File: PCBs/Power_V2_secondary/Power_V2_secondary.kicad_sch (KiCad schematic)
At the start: 15 parts, among them IC7 ACS712ELCTR-20A-T, J1 PCIE-164-02-F-D-TH-TR, J2 Conn_01x08, J8 Conn_01x02, U1 01530007Z

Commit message: follow up changes from meeting
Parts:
- removed J2: Conn_01x08, TerminalBlock:TerminalBlock_MaiXu_MX126-5.0-08P_1x08_P5.00mm, symbol Connector_Generic:Conn_01x08
- added J2: Conn_01x10, TerminalBlock:TerminalBlock_MaiXu_MX126-5.0-10P_1x10_P5.00mm, symbol Connector_Generic:Conn_01x10
- H1, H2: footprint MountingHole:MountingHole_2.5mm -> MountingHole:MountingHole_2.7mm_M2.5_DIN965_Pad_TopBottom
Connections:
- net 14V8_OUT_PROTECTED: now also J2.10 (Pin_10), J2.2 (Pin_2), J2.4 (Pin_4), J2.6 (Pin_6), J2.8 (Pin_8)
- net GND: now also J2.1 (Pin_1), J2.3 (Pin_3), J2.5 (Pin_5), J2.7 (Pin_7), J2.9 (Pin_9)
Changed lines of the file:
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@@
 	(rectangle
 		(start 38.1 133.35)
-		(end 85.09 175.26)
+		(end 85.09 180.34)
 		(stroke
 			(width 0)
@@
 	(wire
 		(pts
+			(xy 62.23 165.1) (xy 63.5 165.1)
+		)
+		(stroke
+			(width 0)
+			(type default)
+		)
+	)
+	(wire
+		(pts
 			(xy 218.44 101.6) (xy 226.06 101.6)
 		)
@@
 	(wire
 		(pts
+			(xy 60.96 167.64) (xy 63.5 167.64)
+		)
+		(stroke
+			(width 0)
+			(type default)
+		)
+	)
+	(wire
+		(pts
 			(xy 193.04 68.58) (xy 193.04 71.12)
 		)
@@
 		)
 	)
+	(label "14V8_OUT_PROTECTED"
+		(at 60.96 167.64 180)
+		(effects
+			(font
+				(size 1.27 1.27)
+			)
+			(justify right bottom)
+		)
+	)
 	(label "14V8"
 		(at 160.02 83.82 180)
@@
 	)
 	(symbol
-		(lib_id "Connector_Generic:Conn_01x08")
-		(at 68.58 152.4 0)
-		(unit 1)
-		(exclude_from_sim no)
-		(in_bom yes)
-		(on_board yes)
-		(dnp no)
-		(fields_autoplaced yes)
-		(property "Reference" "J2"
-			(at 71.12 152.3999 0)
-			(effects
-				(font
-					(size 1.27 1.27)
-				)
-				(justify left)
-			)
-		)
-		(property "Value" "Conn_01x08"
-			(at 71.12 154.9399 0)
-			(effects
-				(font
-					(size 1.27 1.27)
-				)
-				(justify left)
-			)
-		)
-		(property "Footprint" "TerminalBlock:TerminalBlock_MaiXu_MX126-5.0-08P_1x08_P5.00mm"
-			(at 68.58 152.4 0)
-			(effects
-				(font
-					(size 1.27 1.27)
-				)
-				(hide yes)
-			)
-		)
-		(property "Datasheet" "~"
-			(at 68.58 152.4 0)
-			(effects
-				(font
-					(size 1.27 1.27)
-				)
-				(hide yes)
-			)
-		)
-		(property "Description" "Generic connector, single row, 01x08, script generated (kicad-library-utils/schlib/autogen/connector/)"
-			(at 68.58 152.4 0)
-			(effects
-				(font
-					(size 1.27 1.27)
-				)
-				(hide yes)
-			)
-		)
-		(pin "1"
-		)
-		(pin "2"
-		)
-		(pin "5"
-		)
-		(pin "4"
-		)
-		(pin "3"
-		)
-		(pin "8"
-		)
-		(pin "7"
-		)
-		(pin "6"
-		)
-		(instances
-			(project ""
-				(path "/5d5051fd-2bba-4f17-ac84-ab8502b20b0d"
-					(reference "J2")
-					(unit 1)
-				)
-			)
-		)
-	)
-	(symbol
 		(lib_id "power:GND")
 		(at 251.46 113.03 90)
@@
 	)
 	(symbol
+		(lib_id "Connector_Generic:Conn_01x10")
+		(at 68.58 154.94 0)
+		(unit 1)
+		(exclude_from_sim no)
+		(in_bom yes)
+		(on_board yes)
+		(dnp no)
+		(fields_autoplaced yes)
+		(property "Reference" "J2"
+			(at 71.12 154.9399 0)
+			(effects
+				(font
+					(size 1.27 1.27)
+				)
+				(justify left)
+			)
+		)
+		(property "Value" "Conn_01x10"
+			(at 71.12 157.4799 0)
+			(effects
+				(font
+					(size 1.27 1.27)
+				)
+				(justify left)
+			)
+		)
+		(property "Footprint" "TerminalBlock:TerminalBlock_MaiXu_MX126-5.0-10P_1x10_P5.00mm"
+			(at 68.58 154.94 0)
+			(effects
+				(font
+					(size 1.27 1.27)
+				)
+				(hide yes)
+			)
+		)
+		(property "Datasheet" "~"
+			(at 68.58 154.94 0)
+			(effects
+				(font
+					(size 1.27 1.27)
+				)
+				(hide yes)
+			)
+		)
+		(property "Description" "Generic connector, single row, 01x10, script generated (kicad-library-utils/schlib/autogen/connector/)"
+			(at 68.58 154.94 0)
+			(effects
+				(font
+					(size 1.27 1.27)
+				)
+				(hide yes)
+			)
+		)
+		(pin "3"
+		)
+		(pin "1"
+		)
+		(pin "2"
+		)
+		(pin "4"
+		)
+		(pin "5"
+		)
+		(pin "6"
+		)
+		(pin "7"
+		)
+		(pin "9"
+		)
+		(pin "8"
+		)
+		(pin "10"
+		)
+		(instances
+			(project ""
+				(path "/5d5051fd-2bba-4f17-ac84-ab8502b20b0d"
+					(reference "J2")
+					(unit 1)
+				)
+			)
+		)
+	)
+	(symbol
 		(lib_id "power:GND")
 		(at 251.46 82.55 90)
@@
 	)
 	(symbol
+		(lib_id "power:GND")
+		(at 62.23 165.1 270)
+		(unit 1)
+		(exclude_from_sim no)
+		(in_bom yes)
+		(on_board yes)
+		(dnp no)
+		(fields_autoplaced yes)
+		(property "Reference" "#PWR056"
+			(at 55.88 165.1 0)
+			(effects
+				(font
+					(size 1.27 1.27)
+				)
+				(hide yes)
+			)
+		)
+		(property "Value" "GND"
+			(at 58.42 165.0999 90)
+			(effects
+				(font
+					(size 1.27 1.27)
+				)
+				(justify right)
+			)
+		)
+		(property "Footprint" ""
+			(at 62.23 165.1 0)
+			(effects
+				(font
+					(size 1.27 1.27)
+				)
+				(hide yes)
+			)
+		)
+		(property "Datasheet" ""
+			(at 62.23 165.1 0)
+			(effects
+				(font
+					(size 1.27 1.27)
+				)
+				(hide yes)
+			)
+		)
+		(property "Description" "Power symbol creates a global label with name \"GND\" , ground"
+			(at 62.23 165.1 0)
+			(effects
+				(font
+					(size 1.27 1.27)
+				)
+				(hide yes)
+			)
+		)
+		(pin "1"
+		)
+		(instances
+			(project "Power_V2_secondary"
+				(path "/5d5051fd-2bba-4f17-ac84-ab8502b20b0d"
+					(reference "#PWR056")
+					(unit 1)
+				)
+			)
+		)
+	)
+	(symbol
 		(lib_id "Mechanical:MountingHole")
 		(at 107.95 80.01 0)
@@
 			)
 		)
-		(property "Footprint" "MountingHole:MountingHole_2.5mm"
+		(property "Footprint" "MountingHole:MountingHole_2.7mm_M2.5_DIN965_Pad_TopBottom"
 			(at 107.95 80.01 0)
 			(effects
@@
 			)
 		)
-		(property "Footprint" "MountingHole:MountingHole_2.5mm"
+		(property "Footprint" "MountingHole:MountingHole_2.7mm_M2.5_DIN965_Pad_TopBottom"
 			(at 92.71 80.01 0)
 			(effects

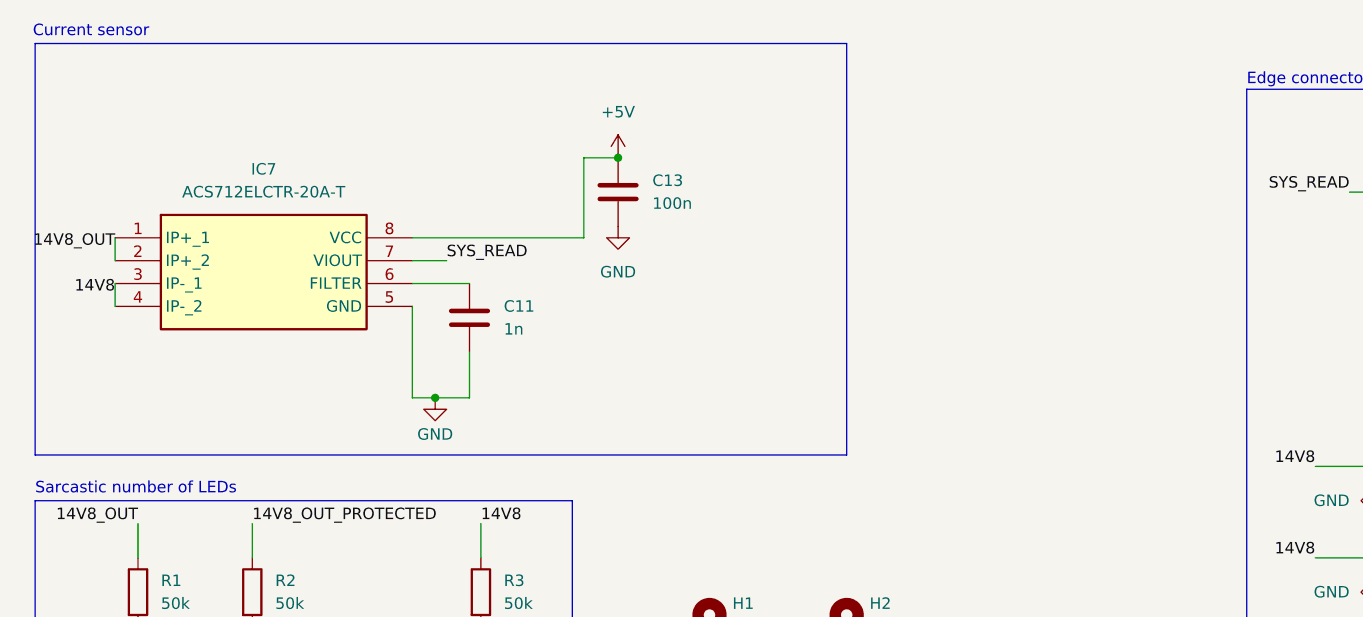
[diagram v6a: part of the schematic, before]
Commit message: 12 to 5V regulator added
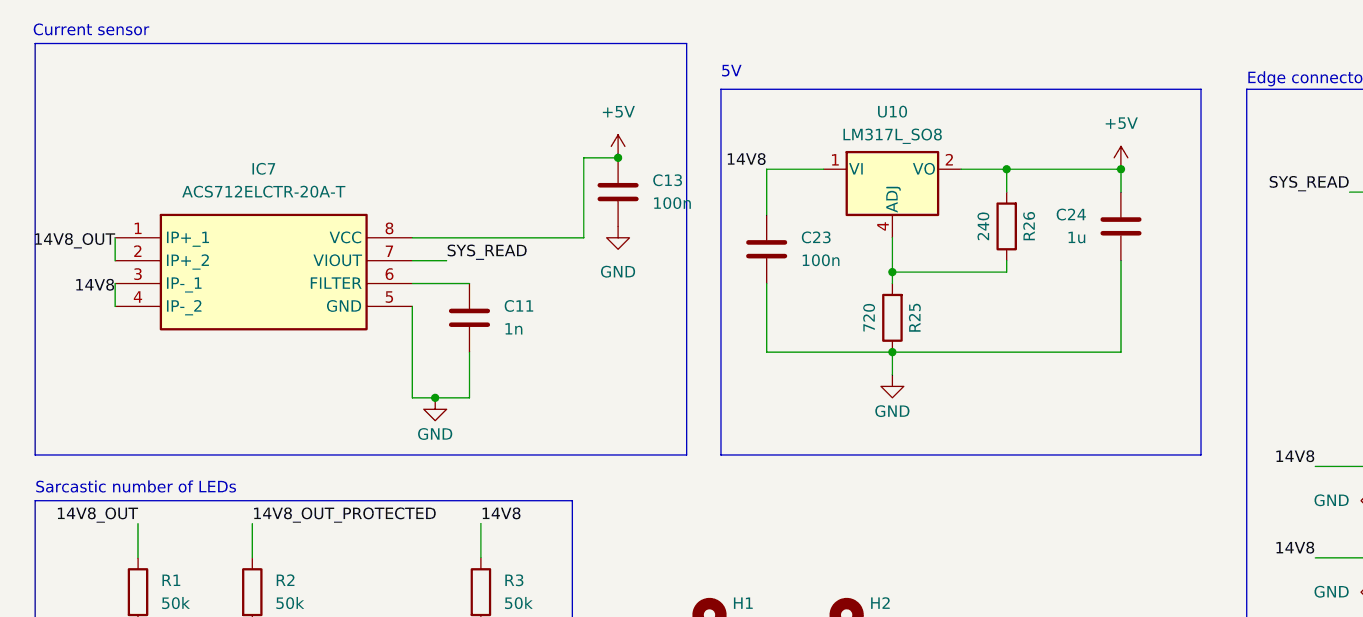
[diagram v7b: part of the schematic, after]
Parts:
- added C23: 100n, Capacitor_SMD:C_0805_2012Metric, symbol Device:C
- added C24: 1u, Capacitor_SMD:C_0805_2012Metric, symbol Device:C
- added R25: 720, Resistor_SMD:R_0805_2012Metric, symbol Device:R
- added R26: 240, Resistor_SMD:R_0805_2012Metric, symbol Device:R
- added U10: LM317L_SO8, Package_SO:SOIC-8_3.9x4.9mm_P1.27mm, symbol Regulator_Linear:LM317L_SO8
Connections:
- net +5V: now also C24.1, R26.2, U10.2 (VO), U10.3 (VO), U10.6 (VO), U10.7 (VO)
- net 14V8: now also C23.1, U10.1 (VI)
- net GND: now also C23.2, C24.2, R25.1
- new net: R25.2, R26.1, U10.4 (ADJ)
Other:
- note added: "5V"
